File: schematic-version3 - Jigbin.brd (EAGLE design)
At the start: 47 x 28 mm, 54 parts, among them J2 FTDI_DEVICE, M1 WIRELESS-NRF24L01, Q1 8MHz, T1 NMOS, T2 NMOS, T3 NMOS, T4 NMOS, U1 ATMEGA328P_TQFP, U2 GY-521MPU6050

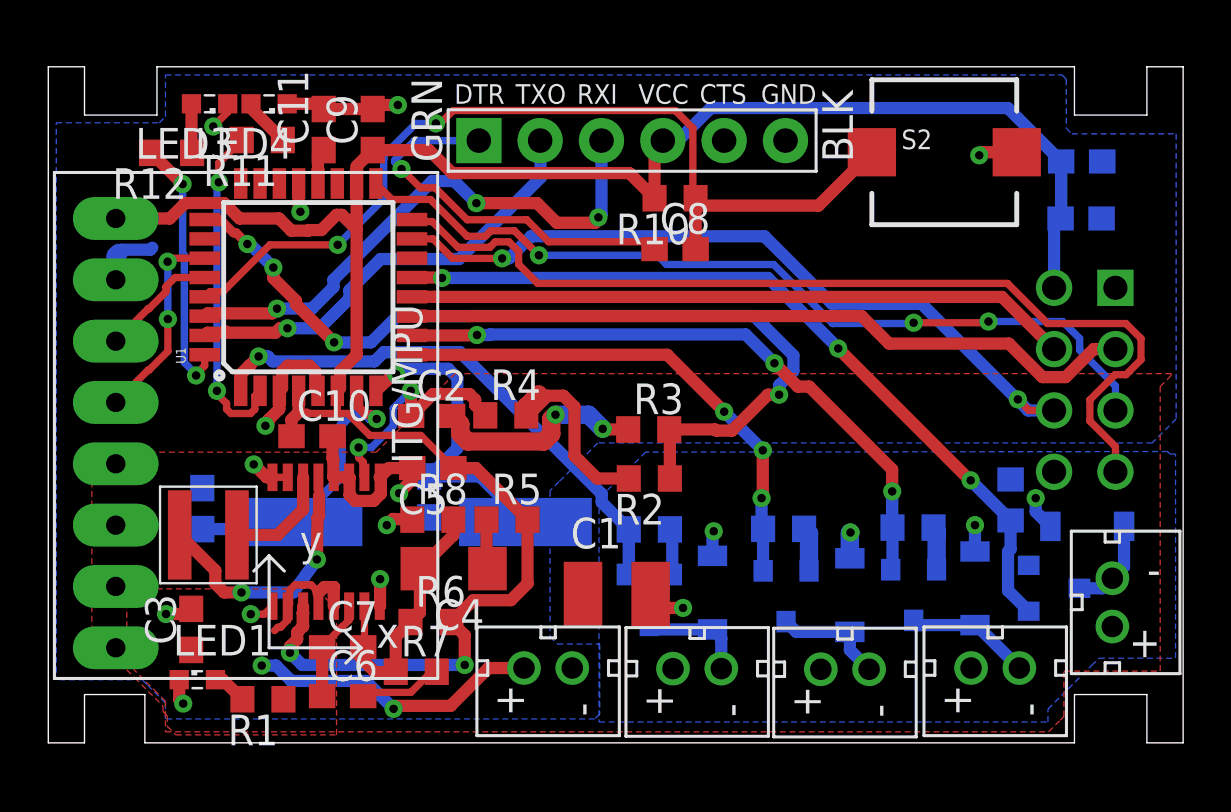
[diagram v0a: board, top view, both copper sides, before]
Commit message: Another draft
Radio on top, IMU on bottom. Ground plane on bottom. Left half of top plane is PWR, for motor needs. Right half of top plane is regulated output, for MCU, radio, and IMU needs.
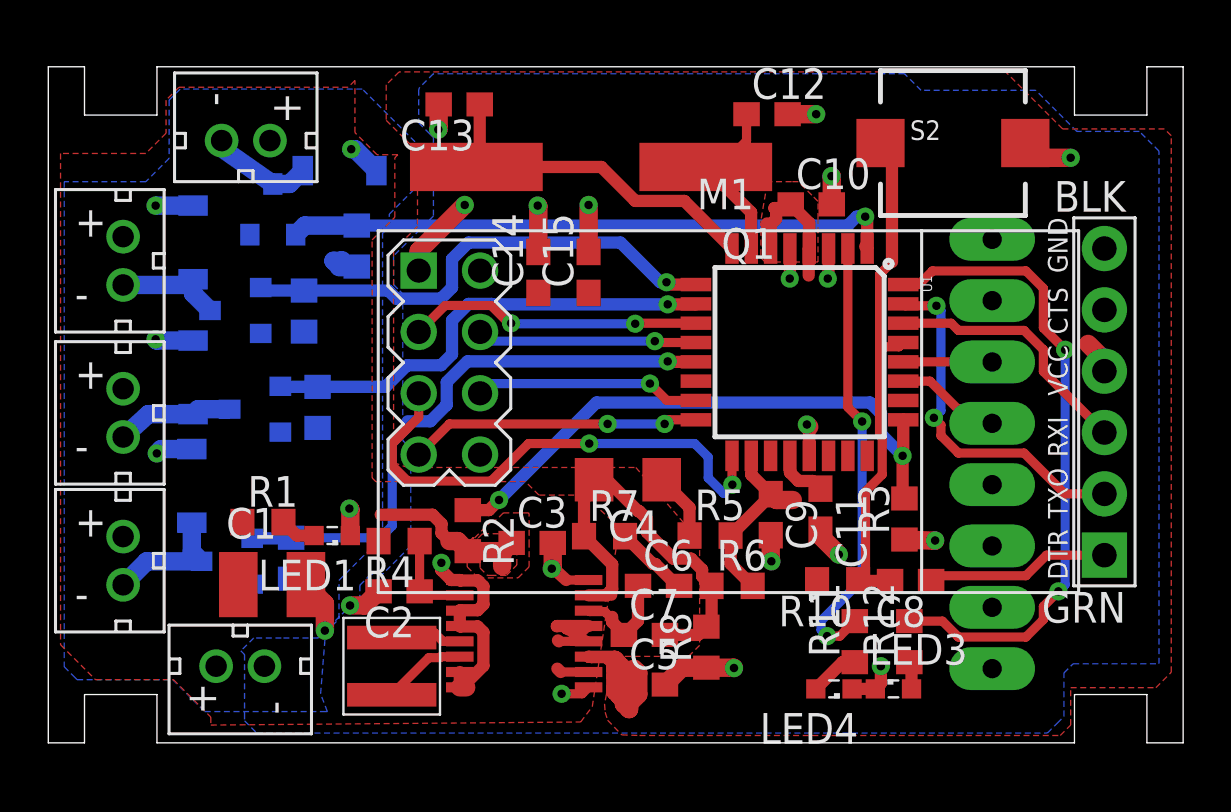
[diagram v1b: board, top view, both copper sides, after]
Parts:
- moved U$13 41.0 mm to (3.10, 7.54), turned to 0 degrees
- moved U$10 37.6 mm to (3.10, 13.7), turned to 0 degrees
- moved LED3 37.3 mm to (35.0, 2.24), turned to 0 degrees
- moved D4 37.1 mm to (5.94, 10.6), turned to 0 degrees
- moved R12 36.7 mm to (35.7, 4.19), turned to 90 degrees
- moved U$7 34.4 mm to (3.10, 20.0), turned to 0 degrees
- moved T4 34.2 mm to (7.44, 7.52), turned to 270 degrees
- moved LED4 33.7 mm to (32.5, 2.24)
- moved D3 33.5 mm to (5.99, 15.1)
- moved R11 32.2 mm to (33.4, 4.19), turned to 90 degrees
- moved D2 30.9 mm to (5.99, 20.7)
- moved R16 29.9 mm to (10.1, 7.65), turned to 90 degrees
- moved U$4 28.8 mm to (8.18, 24.9), turned to 270 degrees
- moved C12 28.5 mm to (29.8, 26.0), flipped to the top, turned to 0 degrees
- moved T3 28.3 mm to (8.61, 13.8), turned to 270 degrees
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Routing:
- net V_REG_OUT: track 93.3 -> 26.2 mm, vias 2 -> 0
- net MISO: track 39.8 -> 12.1 mm, vias 0 -> 2
- net MOSI: track 32.0 -> 9.40 mm, vias 2 -> 1
- net N$2: track 40.5 -> 21.9 mm, vias 2 -> 0
- net CE: track 30.7 -> 12.3 mm, vias 0 -> 2
- net CSN: track 27.5 -> 9.12 mm, vias 0 -> 1
- net DEBUG_LED1: track 11.0 -> 26.9 mm
- net SCK: track 35.7 -> 21.1 mm, vias 3 -> 2
- net V_BAT: track 37.1 -> 24.6 mm, vias 4 -> 2
- net RXD: track 22.9 -> 10.7 mm, vias 3 -> 0
- net PWR: track 30.7 -> 19.3 mm, vias 6 -> 4
- net PWM4: track 33.1 -> 24.1 mm, vias 3 -> 1
- net DTR: track 16.2 -> 7.62 mm, vias 1 -> 0
- net N$8: track 11.2 -> 3.06 mm, vias 2 -> 0
- net PWM3: track 26.4 -> 19.5 mm, vias 3 -> 1
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- added copper zone on layer 1, net V_REG_OUT
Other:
- outline, holes or cut-outs redrawn
